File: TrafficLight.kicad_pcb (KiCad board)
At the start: 2 copper layers, 100 x 100 mm, 3 parts, among them J1 Conn_01x02

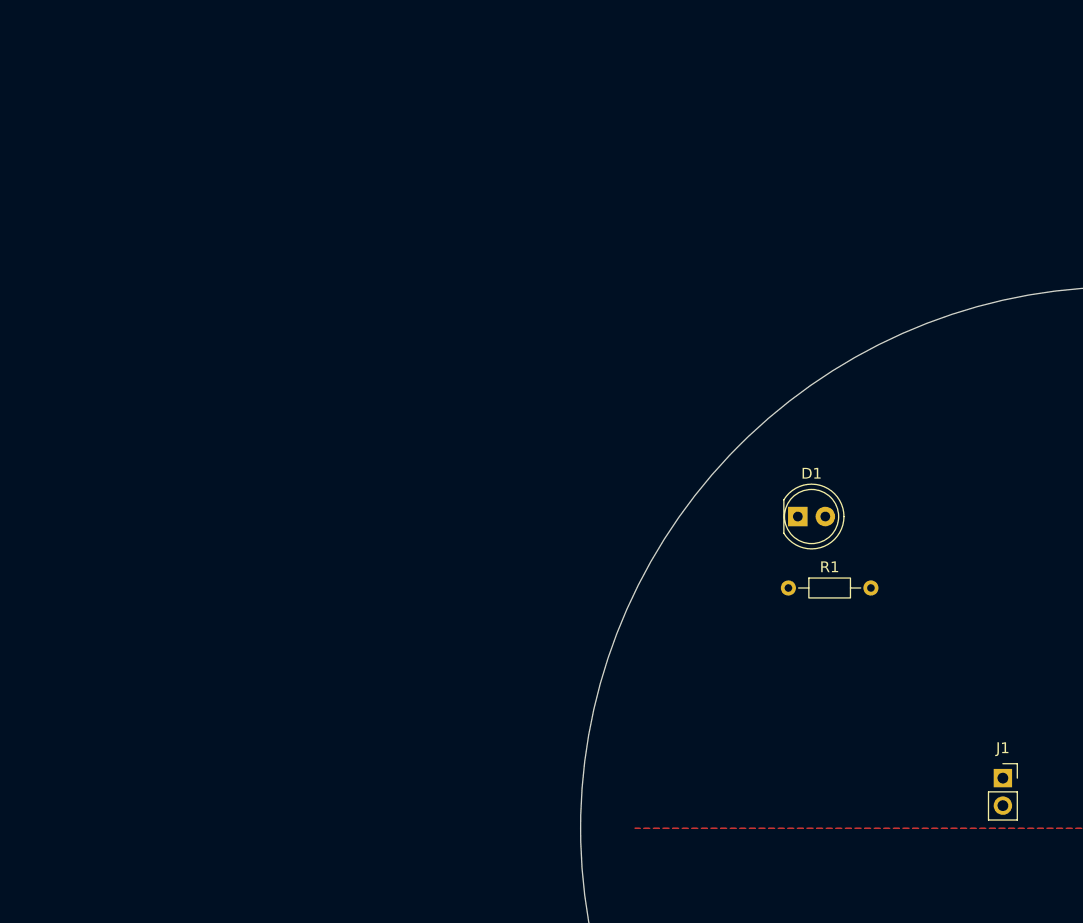
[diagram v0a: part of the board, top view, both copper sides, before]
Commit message: update schematic and place leds
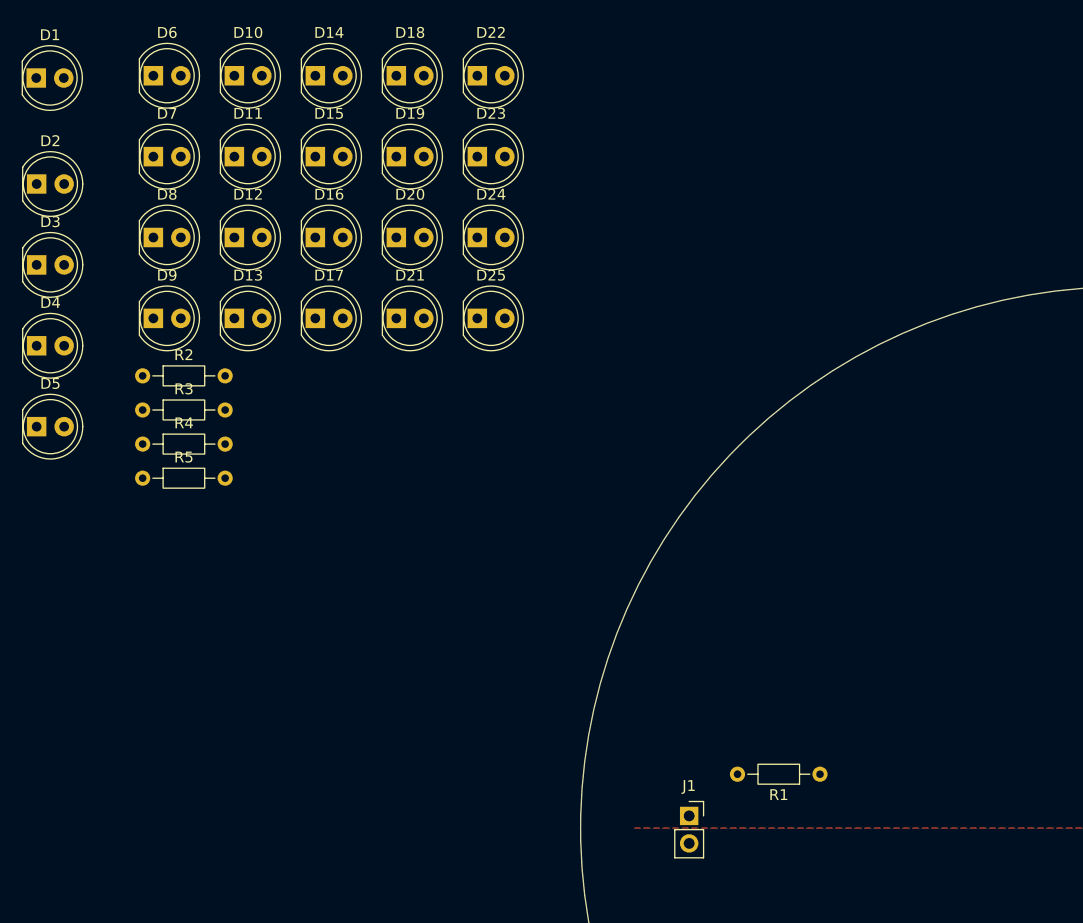
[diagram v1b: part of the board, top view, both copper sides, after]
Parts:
- added D10: LED, LED_THT:LED_D5.0mm, F.Cu at (68.0, 30.5)
- added D11: LED, LED_THT:LED_D5.0mm, F.Cu at (68.0, 38.0)
- added D12: LED, LED_THT:LED_D5.0mm, F.Cu at (68.0, 45.4)
- added D13: LED, LED_THT:LED_D5.0mm, F.Cu at (68.0, 52.9)
- added D14: LED, LED_THT:LED_D5.0mm, F.Cu at (75.5, 30.5)
- added D15: LED, LED_THT:LED_D5.0mm, F.Cu at (75.5, 38.0)
- added D16: LED, LED_THT:LED_D5.0mm, F.Cu at (75.5, 45.4)
- added D17: LED, LED_THT:LED_D5.0mm, F.Cu at (75.5, 52.9)
- added D18: LED, LED_THT:LED_D5.0mm, F.Cu at (83.0, 30.5)
- added D19: LED, LED_THT:LED_D5.0mm, F.Cu at (83.0, 38.0)
- added D2: LED, LED_THT:LED_D5.0mm, F.Cu at (49.8, 40.5)
- added D20: LED, LED_THT:LED_D5.0mm, F.Cu at (83.0, 45.4)
- added D21: LED, LED_THT:LED_D5.0mm, F.Cu at (83.0, 52.9)
- added D22: LED, LED_THT:LED_D5.0mm, F.Cu at (90.5, 30.5)
- added D23: LED, LED_THT:LED_D5.0mm, F.Cu at (90.5, 38.0)
- added D24: LED, LED_THT:LED_D5.0mm, F.Cu at (90.5, 45.4)
- added D25: LED, LED_THT:LED_D5.0mm, F.Cu at (90.5, 52.9)
- added D3: LED, LED_THT:LED_D5.0mm, F.Cu at (49.8, 48.0)
- added D4: LED, LED_THT:LED_D5.0mm, F.Cu at (49.8, 55.4)
- added D5: LED, LED_THT:LED_D5.0mm, F.Cu at (49.8, 62.9)
- added D6: LED, LED_THT:LED_D5.0mm, F.Cu at (60.5, 30.5)
- added D7: LED, LED_THT:LED_D5.0mm, F.Cu at (60.5, 38.0)
- added D8: LED, LED_THT:LED_D5.0mm, F.Cu at (60.5, 45.4)
- added D9: LED, LED_THT:LED_D5.0mm, F.Cu at (60.5, 52.9)
- added R2: 4k7, Resistor_THT:R_Axial_DIN0204_L3.6mm_D1.6mm_P7.62mm_Horizontal, F.Cu at (59.5, 58.2)
- added R3: 4k7, Resistor_THT:R_Axial_DIN0204_L3.6mm_D1.6mm_P7.62mm_Horizontal, F.Cu at (59.5, 61.4)
- added R4: 4k7, Resistor_THT:R_Axial_DIN0204_L3.6mm_D1.6mm_P7.62mm_Horizontal, F.Cu at (59.5, 64.5)
- added R5: 4k7, Resistor_THT:R_Axial_DIN0204_L3.6mm_D1.6mm_P7.62mm_Horizontal, F.Cu at (59.5, 67.7)
- moved D1 81.2 mm to (49.7, 30.7)
- moved J1 29.2 mm to (110.0, 98.8)
- moved R1 17.4 mm to (122.1, 95.0), turned to 180 degrees
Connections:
- D1 pad 1: GND -> Net-(D1-K)

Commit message: try to plot the points in raster
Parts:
- moved D5 132.7 mm to (181.2, 81.2)
- moved D15 126.9 mm to (186.2, 100.0)
- moved D4 118.4 mm to (167.5, 67.5)
- moved D14 118.3 mm to (171.2, 100.0)
- moved D24 116.3 mm to (167.5, 132.5)
- moved D10 115.9 mm to (168.2, 88.7)
- moved D23 115.2 mm to (148.7, 137.3)
- moved D18 113.1 mm to (148.7, 122.5)
- moved D19 112.2 mm to (160.0, 119.5)
- moved D25 112.1 mm to (181.2, 118.7)
- moved D22 109.6 mm to (129.9, 132.7)
- moved D20 107.7 mm to (168.2, 111.3)
- moved D9 103.1 mm to (159.9, 80.5)
- moved D3 100.0 mm to (148.7, 62.5)
- moved D13 100.0 mm to (156.2, 100.0)
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
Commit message: save project
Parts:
- moved J1 30.4 mm to (74.7, 96.7)
- moved R1 30.4 mm to (79.7, 87.9)
- moved R2 30.4 mm to (79.7, 92.9)
- moved R3 30.4 mm to (79.7, 97.9)
- moved R4 30.4 mm to (79.7, 102.9)
- moved R5 30.4 mm to (79.7, 107.9)
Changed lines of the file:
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@@
 	(footprint "Resistor_THT:R_Axial_DIN0204_L3.6mm_D1.6mm_P7.62mm_Horizontal"
 		(layer "F.Cu")
-		(at 110 100)
+		(at 79.69 97.9)
 		(descr "Resistor, Axial_DIN0204 series, Axial, Horizontal, pin pitch=7.62mm, 0.167W, length*diameter=3.6*1.6mm^2, http://cdn-reichelt.de/documents/datenblatt/B400/1_4W%23YAG.pdf")
 		(tags "Resistor Axial_DIN0204 series Axial Horizontal pin pitch 7.62mm 0.167W length 3.6mm diameter 1.6mm")
@@
 	(footprint "Resistor_THT:R_Axial_DIN0204_L3.6mm_D1.6mm_P7.62mm_Horizontal"
 		(layer "F.Cu")
-		(at 110 90)
+		(at 79.69 87.9)
 		(descr "Resistor, Axial_DIN0204 series, Axial, Horizontal, pin pitch=7.62mm, 0.167W, length*diameter=3.6*1.6mm^2, http://cdn-reichelt.de/documents/datenblatt/B400/1_4W%23YAG.pdf")
 		(tags "Resistor Axial_DIN0204 series Axial Horizontal pin pitch 7.62mm 0.167W length 3.6mm diameter 1.6mm")
@@
 	(footprint "Connector_PinSocket_2.54mm:PinSocket_1x02_P2.54mm_Vertical"
 		(layer "F.Cu")
-		(at 105.025 98.75)
+		(at 74.715 96.65)
 		(descr "Through hole straight socket strip, 1x02, 2.54mm pitch, single row (from Kicad 4.0.7), script generated")
 		(tags "Through hole socket strip THT 1x02 2.54mm single row")
@@
 	(footprint "Resistor_THT:R_Axial_DIN0204_L3.6mm_D1.6mm_P7.62mm_Horizontal"
 		(layer "F.Cu")
-		(at 110 105)
+		(at 79.69 102.9)
 		(descr "Resistor, Axial_DIN0204 series, Axial, Horizontal, pin pitch=7.62mm, 0.167W, length*diameter=3.6*1.6mm^2, http://cdn-reichelt.de/documents/datenblatt/B400/1_4W%23YAG.pdf")
 		(tags "Resistor Axial_DIN0204 series Axial Horizontal pin pitch 7.62mm 0.167W length 3.6mm diameter 1.6mm")
@@
 	(footprint "Resistor_THT:R_Axial_DIN0204_L3.6mm_D1.6mm_P7.62mm_Horizontal"
 		(layer "F.Cu")
-		(at 110 110)
+		(at 79.69 107.9)
 		(descr "Resistor, Axial_DIN0204 series, Axial, Horizontal, pin pitch=7.62mm, 0.167W, length*diameter=3.6*1.6mm^2, http://cdn-reichelt.de/documents/datenblatt/B400/1_4W%23YAG.pdf")
 		(tags "Resistor Axial_DIN0204 series Axial Horizontal pin pitch 7.62mm 0.167W length 3.6mm diameter 1.6mm")
@@
 	(footprint "Resistor_THT:R_Axial_DIN0204_L3.6mm_D1.6mm_P7.62mm_Horizontal"
 		(layer "F.Cu")
-		(at 110 95)
+		(at 79.69 92.9)
 		(descr "Resistor, Axial_DIN0204 series, Axial, Horizontal, pin pitch=7.62mm, 0.167W, length*diameter=3.6*1.6mm^2, http://cdn-reichelt.de/documents/datenblatt/B400/1_4W%23YAG.pdf")
 		(tags "Resistor Axial_DIN0204 series Axial Horizontal pin pitch 7.62mm 0.167W length 3.6mm diameter 1.6mm")
@@
 	)
 	(gr_line
-		(start 106.69873 75)
-		(end 193.30127 125)
+		(start 100 60)
+		(end 200 60)
+		(stroke
+			(width 0.1)
+			(type solid)
+		)
+		(layer "Dwgs.User")
+	)
+	(gr_line
+		(start 100 140)
+		(end 200 140)
 		(stroke
 			(width 0.1)
@@
 	)
 	(gr_line
-		(start 175 56.69873)
-		(end 125 143.30127)
+		(start 100 80)
+		(end 200 80)
+		(stroke
+			(width 0.1)
+			(type solid)
+		)
+		(layer "Dwgs.User")
+	)
+	(gr_line
+		(start 170 50)
+		(end 170 150)
 		(stroke
 			(width 0.1)
@@
 	)
 	(gr_line
-		(start 125 56.69873)
-		(end 175 143.30127)
+		(start 130 50)
+		(end 130 150)
+		(stroke
+			(width 0.1)
+			(type solid)
+		)
+		(layer "Dwgs.User")
+	)
+	(gr_line
+		(start 110 50)
+		(end 110 150)
 		(stroke
 			(width 0.1)
@@
 	)
 	(gr_line
-		(start 193.30127 75)
-		(end 106.69873 125)
+		(start 190 50)
+		(end 190 150)
+		(stroke
+			(width 0.1)
+			(type solid)
+		)
+		(layer "Dwgs.User")
+	)
+	(gr_line
+		(start 100 120)
+		(end 200 120)
 		(stroke
 			(width 0.1)

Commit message: remove files
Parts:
- removed D10, D15, D20, D24, D25, D5: LED, LED_THT:LED_D5.0mm
- moved J1 84.2 mm to (148.8, 56.5), turned to 90 degrees
- moved D9 18.9 mm to (178.7, 82.7)
- moved D11 17.2 mm to (108.7, 100.0)
- moved D12 12.1 mm to (148.5, 109.6)
- moved D8 11.3 mm to (158.7, 82.7)
- moved D6 11.2 mm to (128.7, 100.0)
- moved D14 8.89 mm to (176.8, 106.9)
- moved D13 8.64 mm to (160.3, 107.6)
- moved D3 2.90 mm to (148.7, 65.4)
- moved D1 2.87 mm to (118.7, 82.7)
- moved D7 2.51 mm to (138.7, 82.7)
- moved D2 2.46 mm to (128.7, 65.4)
- moved D4 2.42 mm to (168.7, 65.4)
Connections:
- D14 pad 1: Net-(D14-K) -> GND
- D19 pad 1: Net-(D19-K) -> GND
- D23 pad 1: Net-(D23-K) -> GND
- D4 pad 1: Net-(D4-K) -> GND
- D9 pad 1: Net-(D10-A) -> GND
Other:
- board size 100 x 100 mm -> 60 x 60 mm
